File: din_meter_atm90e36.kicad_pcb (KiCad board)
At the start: 4 copper layers, 32 x 31.1 mm, 72 parts, among them IC1 ATM90E36_ATM90E36, IC2 ATM90E36_ATM90E36, J7 Conn_01x10, J8 Conn_02x18_Row_Letter_First, Y1 Crystal_GND24, Y2 Crystal_GND24

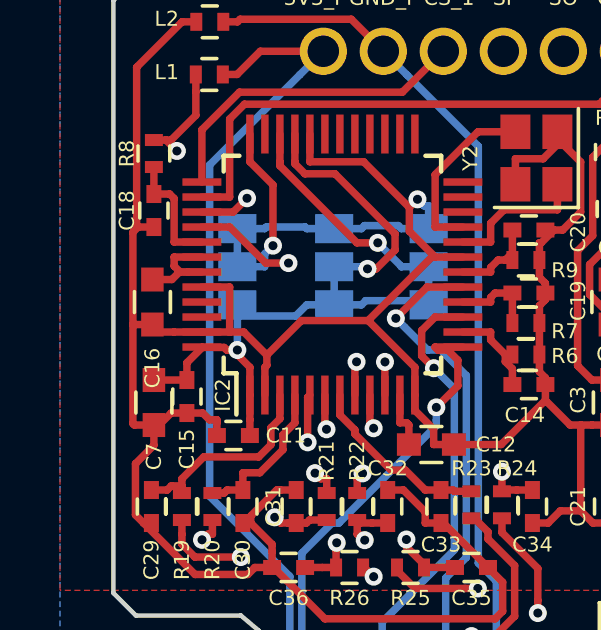
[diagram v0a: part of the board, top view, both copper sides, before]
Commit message: Fixed some silk, add ground plane and HTML BOM
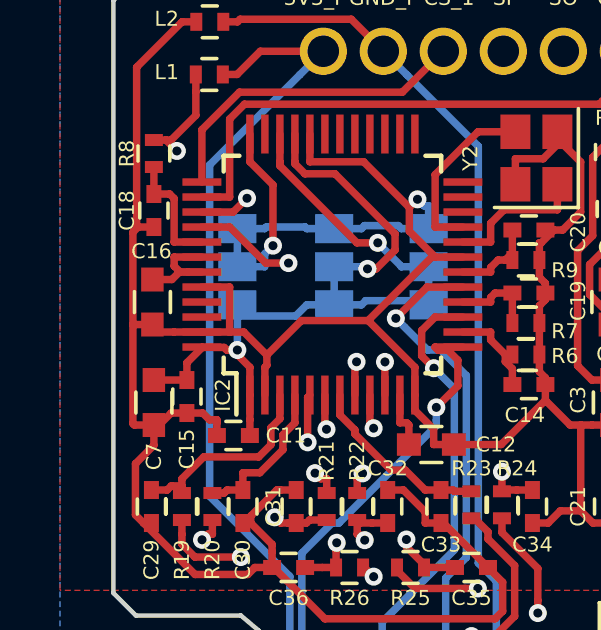
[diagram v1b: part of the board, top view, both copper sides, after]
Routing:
- added copper zone on B.Cu, net GND_ISO
- added copper zone on F.Cu, net GND_ISO
- removed copper zone on B.Cu, net GND
- removed copper zone on F.Cu, net GND
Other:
- board text added: "Dual ATM90E36 Metering v0.2 10/02/2018"
- board text removed: "Dual ATM90E36 Metering v0.1 17/01/2018"

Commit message: Fixed 1k reset resistor to 10k
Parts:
- R8: value 1K -> 10K
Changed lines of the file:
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@@
       (effects (font (size 0.5 0.5) (thickness 0.125)))
     )
-    (fp_text value 1K (at 0 1.45 270) (layer F.Fab)
+    (fp_text value 10K (at 0 1.45 270) (layer F.Fab)
       (effects (font (size 1 1) (thickness 0.15)))
     )
